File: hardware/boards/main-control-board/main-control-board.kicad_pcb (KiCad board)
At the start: 2 copper layers, 122.9 x 33 mm, 7 parts, among them J1 Conn_MAX98357, J2 Conn_OLED, J3 Conn_PCA9685_1, J4 Conn_PCA9685_2, J5 Conn_ESP32_R, J6 Conn_ESP32_L, J7 Conn_USB

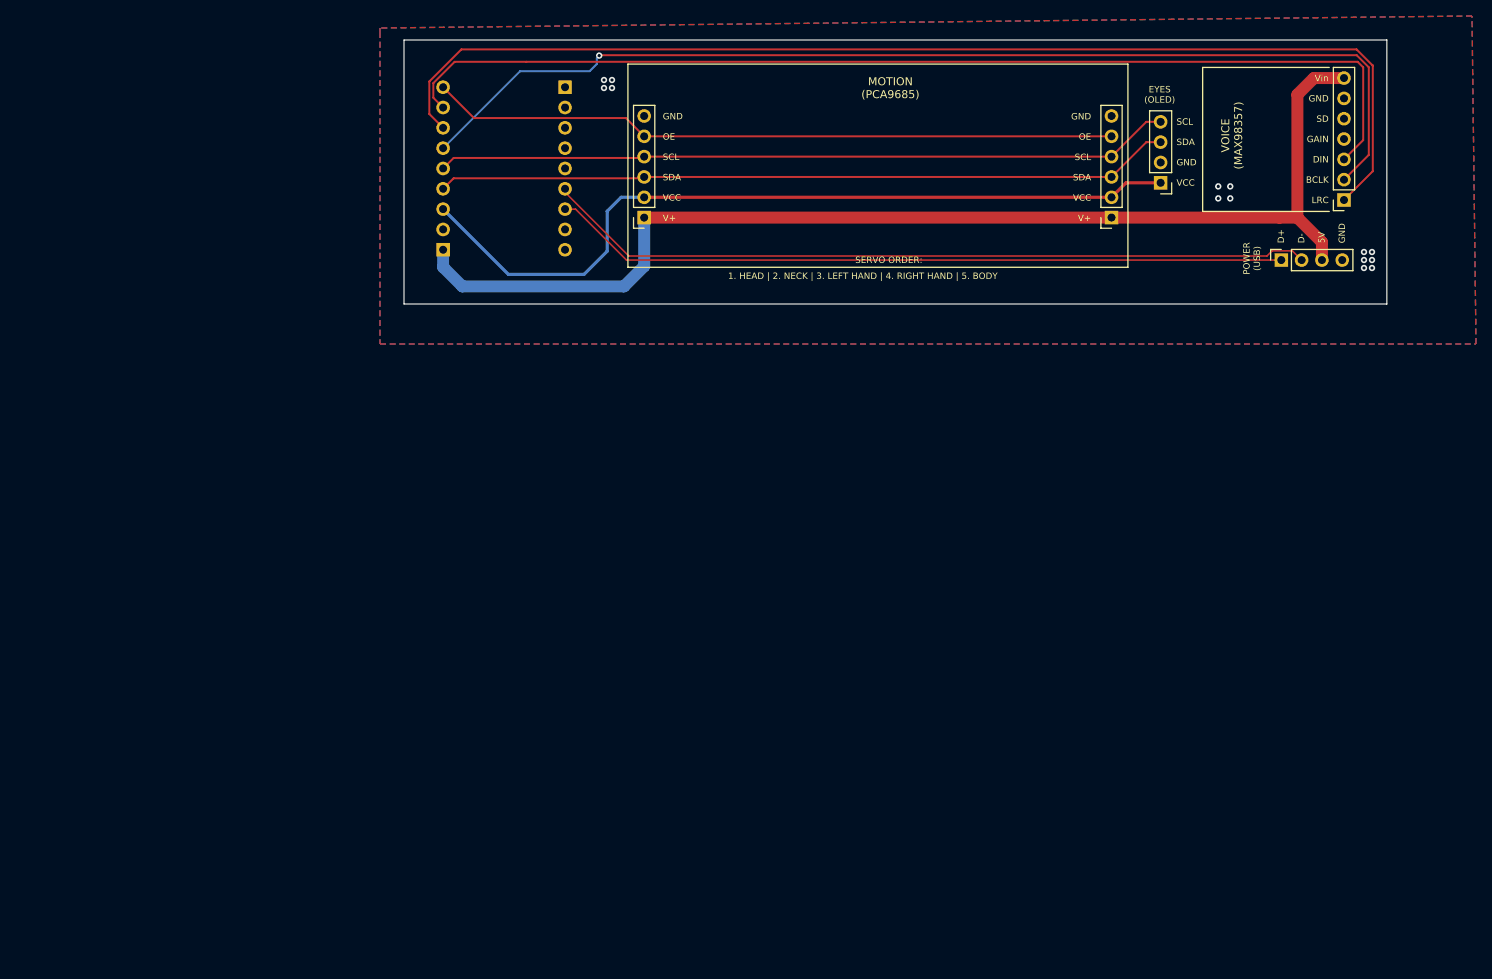
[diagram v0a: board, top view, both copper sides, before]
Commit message: feat(pcb): design integrated PCB for Tiny Engineer electronics (#46, #10)
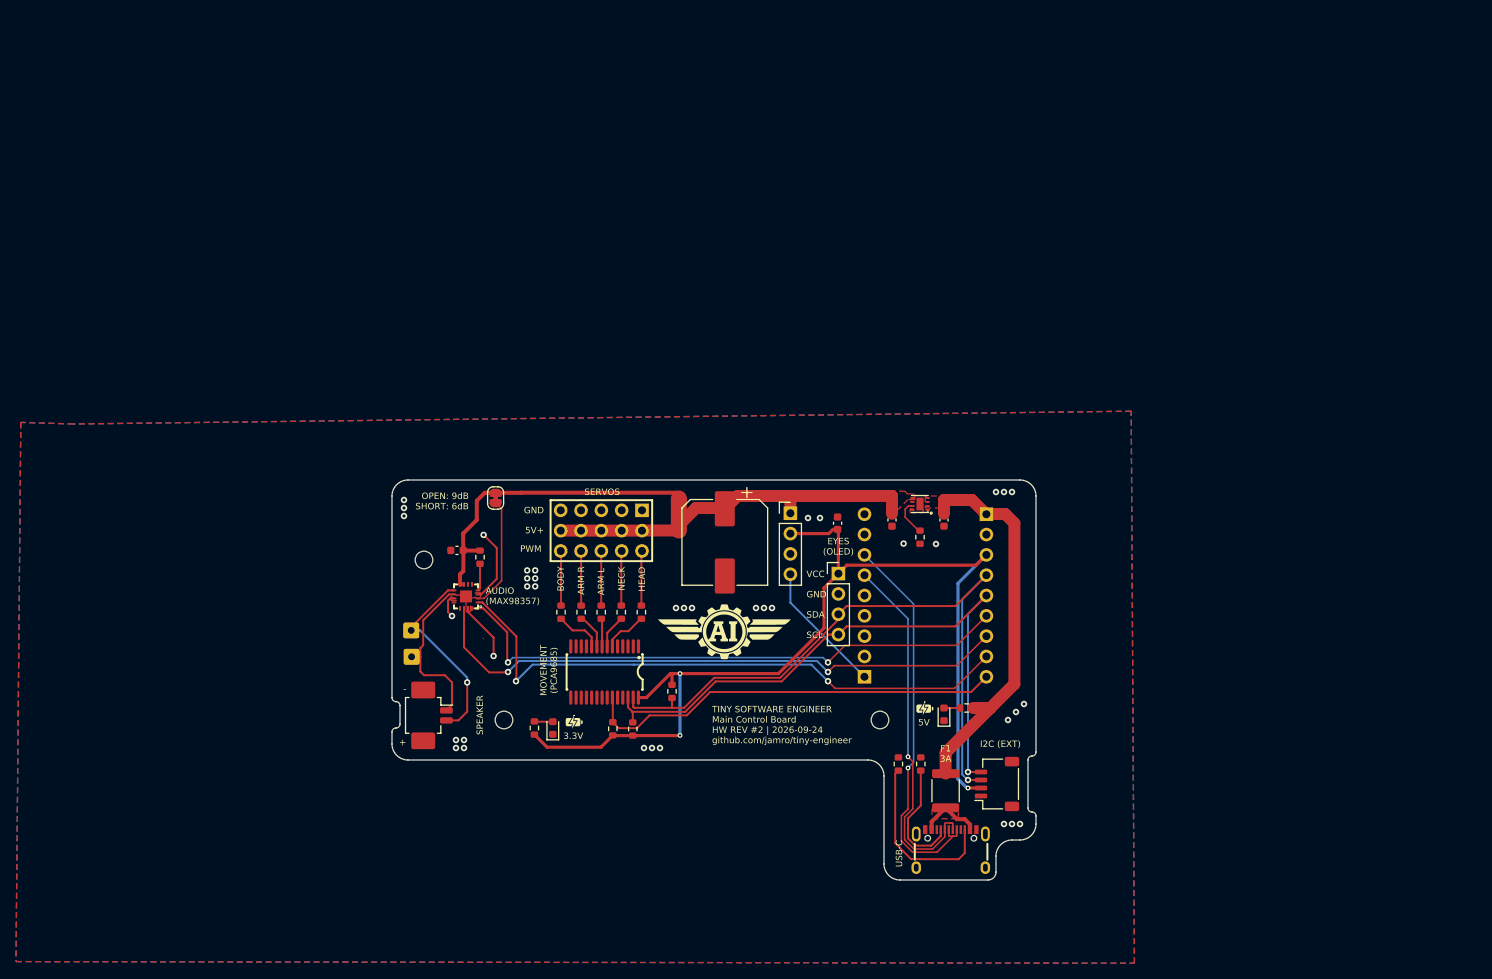
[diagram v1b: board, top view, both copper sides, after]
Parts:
- removed J5: Conn_ESP32_R, Connector_PinSocket_2.54mm:PinSocket_1x09_P2.54mm_Vertical
- removed J6: Conn_ESP32_L, Connector_PinSocket_2.54mm:PinSocket_1x09_P2.54mm_Vertical
- added C1: 100nF, Capacitor_SMD:C_0603_1608Metric, F.Cu at (177.7, 90.4)
- added C2: 1000uF, Capacitor_SMD:CP_Elec_10x10.5, F.Cu at (163.6, 92.8)
- added C3: 100nF, Capacitor_SMD:C_0603_1608Metric, F.Cu at (130.1, 93.8)
- added C4: 100nF, Capacitor_SMD:C_0603_1608Metric, F.Cu at (191.0, 90.0)
- added C5: 100nF, Capacitor_SMD:C_0603_1608Metric, F.Cu at (184.5, 90.0)
- added D1: LED, LED_SMD:LED_0603_1608Metric, F.Cu at (191.0, 114.3)
- added D2: LED, LED_SMD:LED_0603_1608Metric, F.Cu at (142.1, 116.0)
- added F1: 3A PPTC, Fuse:Fuse_1812_4532Metric, F.Cu at (191.2, 123.8)
- added H1: MountingHole, MountingHole:MountingHole_2.2mm_M2, F.Cu at (126.0, 95.0)
- added H2: MountingHole, MountingHole:MountingHole_2.2mm_M2, F.Cu at (136.0, 115.0)
- added H3: MountingHole, MountingHole:MountingHole_2.2mm_M2, F.Cu at (183.0, 115.0)
- added J8: Conn_ESP32_R, Connector_PinSocket_2.54mm:PinSocket_1x09_P2.54mm_Vertical, B.Cu at (181.1, 109.6)
- added JP1: SolderJumper_gain_6dB_limit, Jumper:SolderJumper-2_P1.3mm_Bridged_RoundedPad1.0x1.5mm, F.Cu at (134.9, 87.2)
- added NT1: NetTie_2, NetTie:NetTie-2_SMD_Pad2.0mm, F.Cu at (157.9, 89.3)
- added R1: 5.1k, Resistor_SMD:R_0603_1608Metric, F.Cu at (188.1, 120.5)
- added R10: 220, Resistor_SMD:R_0603_1608Metric, F.Cu at (143.1, 101.5)
- added R11: 2.2k, Resistor_SMD:R_0603_1608Metric, F.Cu at (193.8, 113.5)
- added R12: 1M, Resistor_SMD:R_0603_1608Metric, F.Cu at (133.0, 94.7)
- added R13: 1k, Resistor_SMD:R_0603_1608Metric, F.Cu at (139.8, 116.0)
- added R14: 1k, Resistor_SMD:R_0603_1608Metric, F.Cu at (188.0, 92.2)
- added R2: 5.1k, Resistor_SMD:R_0603_1608Metric, F.Cu at (185.3, 120.5)
- added R3: 10k, Resistor_SMD:R_0603_1608Metric, F.Cu at (149.6, 116.1)
- added R4: 4.7k, Resistor_SMD:R_0603_1608Metric, F.Cu at (152.1, 116.1)
- added R5: 4.7k, Resistor_SMD:R_0603_1608Metric, F.Cu at (157.0, 111.4)
- added R6: 220, Resistor_SMD:R_0603_1608Metric, F.Cu at (153.2, 101.5)
- added R7: 220, Resistor_SMD:R_0603_1608Metric, F.Cu at (150.7, 101.5)
- added R8: 220, Resistor_SMD:R_0603_1608Metric, F.Cu at (148.2, 101.5)
- added R9: 220, Resistor_SMD:R_0603_1608Metric, F.Cu at (145.6, 101.5)
- added TP1: TestPoint, Connector_Wire:SolderWire-0.25sqmm_1x01_D0.65mm_OD2mm, F.Cu at (124.5, 107.1)
- added TP2: TestPoint, Connector_Wire:SolderWire-0.25sqmm_1x01_D0.65mm_OD2mm, F.Cu at (124.4, 103.8)
- added U1: PCA9685PW,118, easyeda:TSSOP-28_L9.7-W4.4-P0.65-LS6.4-TL, F.Cu at (148.6, 109.0)
- added U2: HX PZ2.54-3X5P ZZ, easyeda:HDR-TH_15P-P2.54-V-M-R3-C5-S7.5, F.Cu at (148.2, 91.3)
- added U3: MAX98357AETE+T, easyeda:TQFN-16_L3.0-W3.0-P0.50-BL-EP1.5, F.Cu at (131.2, 99.5)
- added U4: TPS259571DSGR, easyeda:WSON-8_L2.0-W2.0-P0.50-TL-EP, F.Cu at (188.0, 88.0)
- added USB1: TYPE-C 16PIN 2MD, easyeda:USB-C-SMD_TYPE-C-16PIN-2MD-073, F.Cu at (191.8, 131.1)
- J1: value Conn_MAX98357 -> Conn_01x02_Pin_Speaker; footprint Connector_PinSocket_2.54mm:PinSocket_1x07_P2.54mm_Vertical -> Connector_Molex:Molex_PicoBlade_53261-0271_1x02-1MP_P1.25mm_Horizontal
- J3: value Conn_PCA9685_1 -> Conn_extension; footprint Connector_PinSocket_2.54mm:PinSocket_1x06_P2.54mm_Vertical -> Connector_JST:JST_SH_SM04B-SRSS-TB_1x04-1MP_P1.00mm_Horizontal
- J4: value Conn_PCA9685_2 -> Conn_extension_2; footprint Connector_PinSocket_2.54mm:PinSocket_1x06_P2.54mm_Vertical -> Connector_PinHeader_2.54mm:PinHeader_1x04_P2.54mm_Vertical
- J7: value Conn_USB -> Conn_ESP32_L; footprint Connector_PinSocket_2.54mm:PinSocket_1x04_P2.54mm_Vertical -> Connector_PinSocket_2.54mm:PinSocket_1x09_P2.54mm_Vertical; moved to B.Cu
- moved J1 131.5 mm to (126.4, 114.4), turned to -90 degrees
- moved J3 83.4 mm to (197.6, 123.0), turned to 90 degrees
- moved J2 63.3 mm to (177.8, 96.7), turned to 0 degrees
- moved J4 54.6 mm to (171.8, 89.2), turned to 0 degrees
- moved J7 48.7 mm to (196.3, 89.3), turned to 180 degrees
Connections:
- J1 pad 1: /I2S_LRC -> Net-(J1-Pin_1)
- J1 pad 2: /I2S_BCLK -> Net-(J1-Pin_2)
- J3 pad 1: +5V -> GND
- J4 pad 1: +5V -> /PCA/SERVO_5V
- J4 pad 3: /I2C_SDA -> GND
- J4 pad 4: /I2C_SCL -> /ESP32/GP6
- J7 pad 1: /USB_D+ -> +5V
- J7 pad 2: /USB_D- -> GND
- J7 pad 3: +5V -> +3.3V
- J7 pad 4: GND -> /I2C_SDA
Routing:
- net +5V: track 145.7 -> 48.8 mm
- net Net-(J3-Pin_5): track 86.1 -> 0.00 mm
- net /I2S_LRC: track 145.2 -> 74.3 mm, vias 0 -> 2
- net /I2S_BCLK: track 136.9 -> 72.5 mm, vias 1 -> 2
- net /I2S_DIN: track 133.7 -> 74.6 mm, vias 0 -> 2
- net /ESP32/GP5: track 0.00 -> 52.8 mm
- net /USB_D-: track 96.5 -> 45.6 mm, vias 0 -> 1
- net /PCA/SERVO_5V: track 0.00 -> 48.6 mm
- net /USB_D+: track 92.2 -> 49.4 mm, vias 0 -> 1
- net /Audio/AUDIO_5V: track 0.00 -> 39.9 mm
- net +3.3V: track 101.0 -> 126.8 mm, vias 0 -> 3
- net Net-(J1-Pin_2): track 0.00 -> 24.4 mm, vias 0 -> 1
- net Net-(USB1-CC2): track 0.00 -> 22.0 mm
- net Net-(J1-Pin_1): track 0.00 -> 21.1 mm
- net GND: track 0.00 -> 21.0 mm, vias 14 -> 38
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- added copper zone on F.Cu, net +5V
- added copper zone on F.Cu, net /PCA/SERVO_5V
- added copper zone on F.Cu, net /USB/USB_VBUS
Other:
- board size 122.9 x 33 mm -> 80.5 x 50 mm
- board text added: "+"
- board text added: "+3.3V"
- board text added: "+5V"
- board text added: "-"
- board text added: "3.3V"
- board text added: "5V+"
- board text added: "ARM L"
- board text added: "ARM R"
- board text added: "AUDIO (MAX98357)"
- board text added: "BODY"
- board text added: "DO NOT USE ESP USB WHILE BOARD USB IS CONNECTED!"
- board text added: "EXTENSIONS"
- board text added: "F1 3A"
- board text added: "HEAD"
- board text added: "I2C (EXT)"
- board text added: "MOVEMENT (PCA9685)"
- board text added: "NECK"
- board text added: "OPEN: 9dB SHORT: 6dB"
- board text added: "PWM"
- board text added: "SERVOS"
- board text added: "SPEAKER"
- board text added: "TINY SOFTWARE ENGINEER Main Control Board HW REV #2 | 2026-09-24 github.com/jamro/tiny-engineer"
- board text added: "USB-C"
- board text added: "USE JST OR PADS ONLY, NOT BOTH"
- board text removed: "1. HEAD | 2. NECK | 3. LEFT HAND | 4. RIGHT HAND | 5. BODY"
- board text removed: "BCLK"
- board text removed: "D+"
- board text removed: "D-"
- board text removed: "DIN"
- board text removed: "GAIN"
- board text removed: "LRC"
- board text removed: "MOTION (PCA9685)"
- board text removed: "Main Control Board REV #1 | 2026-09-12 github.com/jamro/tiny-engineer"
- board text removed: "OE"
- board text removed: "POWER (USB)"
- board text removed: "SD"
- board text removed: "SERVO ORDER:"
- board text removed: "TINY SOFTWARE ENGINEER"
- board text removed: "V+"
- board text removed: "VOICE (MAX98357)"
- board text removed: "Vin"

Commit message: feat(pcb): update component properties and add missing attributes
- Renamed connection values for ESP32 components to standardize naming.
- Added properties for KiLib_Generator, MPN, and Manufacturer for various components across multiple schematic files.
- Enhanced documentation for component attributes to improve clarity and accessibility in the design process.
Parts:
- J7: value Conn_ESP32_L -> Conn_ESP32
- J8: value Conn_ESP32_R -> Conn_ESP32

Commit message: fix(cad): mark polarization of LEDs in silkscreen
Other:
- board text added: "K"
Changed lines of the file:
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@@
 		(layer "Edge.Cuts")
+	)
+	(gr_text "K"
+		(at 142 118.05 270)
+		(layer "F.SilkS")
+		(effects
+			(font
+				(size 0.6 0.6)
+				(thickness 0.12)
+			)
+		)
+	)
+	(gr_text "K"
+		(at 190.9 116.35 270)
+		(layer "F.SilkS")
+		(effects
+			(font
+				(size 0.6 0.6)
+				(thickness 0.12)
+			)
+		)
 	)
 	(gr_text "TINY SOFTWARE ENGINEER\nMain Control Board\nHW REV #2 | 2026-09-24\ngithub.com/jamro/tiny-engineer"
